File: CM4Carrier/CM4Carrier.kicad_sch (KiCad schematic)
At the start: 0 parts

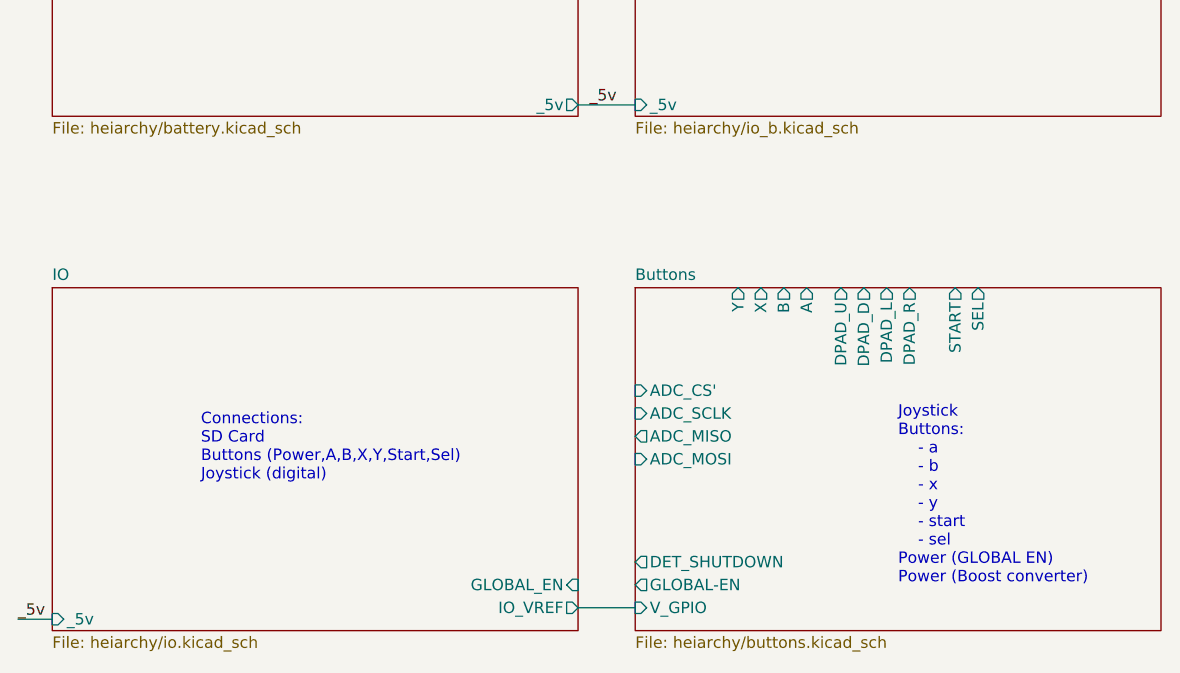
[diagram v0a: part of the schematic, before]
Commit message: footprints  + values
need to do some 3d babeeeeeeeeee
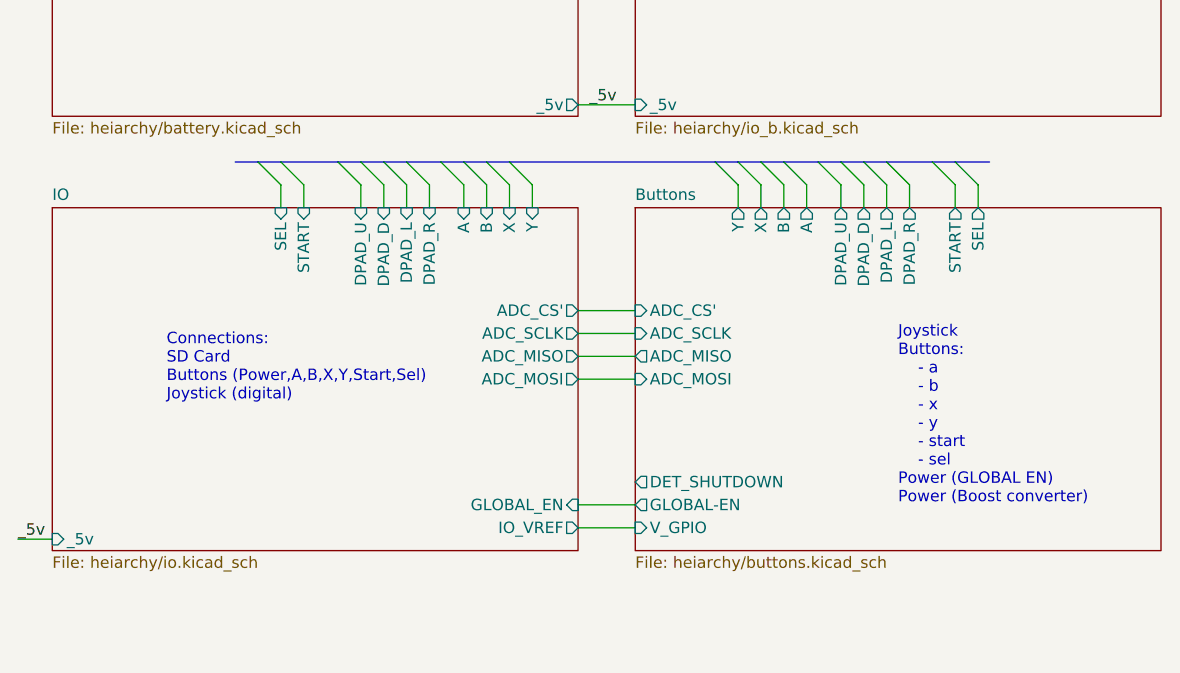
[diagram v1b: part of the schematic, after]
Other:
- sheet IO ports: added A, ADC_CS', ADC_MISO, ADC_MOSI, ADC_SCLK, B, DPAD_D, DPAD_L, DPAD_R, DPAD_U, SEL, START, X, Y; removed none

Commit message: pcb babeee les goooo
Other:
- sheet Battery ports: added ALRT, BATT, FUEL_SCL, FUEL_SDA; removed EN
- sheet Buttons ports: added BATT; removed none
- sheet IO ports: added FUEL_ALRT, FUEL_SCLK, FUEL_SDA; removed none
- sheet IO B ports: added _3.3v; removed none
- title: (none) -> Cm4 battery carrier

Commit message: pcb w proper design
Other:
- note added: "TBF: HEADPHONE JACK / SOUND"
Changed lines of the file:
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@@
     (effects (font (size 1.27 1.27)) (justify left bottom))
+  )
+  (text "TBF: HEADPHONE JACK / SOUND" (at 33.02 39.37 0)
+    (effects (font (size 5.08 5.08)) (justify left bottom))
   )
   (text "Connections:\nSD Card\nButtons (Power,A,B,X,Y,Start,Sel)\nJoystick (digital)\n"

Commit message: LAYOUT DONE!!
:)
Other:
- sheet Battery ports: added BATT_SYSTEM; removed BATT
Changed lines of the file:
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@@
     (stroke (width 0) (type default) (color 0 0 0 0))
   )
-  (wire (pts (xy 152.4 127) (xy 157.48 127))
+  (wire (pts (xy 151.13 127) (xy 157.48 127))
     (stroke (width 0) (type default) (color 0 0 0 0))
   )
@@
     (stroke (width 0) (type default) (color 0 0 0 0))
   )
-  (wire (pts (xy 87.63 49.53) (xy 92.71 49.53))
+  (wire (pts (xy 85.09 49.53) (xy 92.71 49.53))
     (stroke (width 0) (type default) (color 0 0 0 0))
   )
@@
     (effects (font (size 1.27 1.27)) (justify left bottom))
   )
-  (label "BATT" (at 87.63 49.53 0)
+  (label "BATT_S" (at 85.09 49.53 0)
     (effects (font (size 1.27 1.27)) (justify left bottom))
   )
@@
     (effects (font (size 1.27 1.27)) (justify left bottom))
   )
-  (label "BATT" (at 152.4 127 0)
+  (label "BATT_S" (at 151.13 127 0)
     (effects (font (size 1.27 1.27)) (justify left bottom))
   )
@@
       (effects (font (size 1.27 1.27)) (justify left))
     )
-    (pin "BATT" output (at 92.71 49.53 180)
+    (pin "BATT_SYSTEM" output (at 92.71 49.53 180)
       (effects (font (size 1.27 1.27)) (justify left))
     )
@@
       (reference "#PWR042") (unit 1) (value "GND") (footprint "")
     )
+    (path "/1d948cd0-f6e4-4bae-aaaf-c0cfc5cdd7a9/1c3ebfff-ac3c-480a-9097-6cb2c8497089"
+      (reference "#PWR043") (unit 1) (value "GND") (footprint "")
+    )
+    (path "/1d948cd0-f6e4-4bae-aaaf-c0cfc5cdd7a9/39896e95-d5b7-4b2d-91fb-a97d46123782"
+      (reference "#PWR044") (unit 1) (value "GND") (footprint "")
+    )
+    (path "/1d948cd0-f6e4-4bae-aaaf-c0cfc5cdd7a9/731119db-1eb9-4e2e-bea2-451b639aa99a"
+      (reference "#PWR045") (unit 1) (value "GND") (footprint "")
+    )
+    (path "/1d948cd0-f6e4-4bae-aaaf-c0cfc5cdd7a9/1903e911-890a-44bf-8598-6b1ee7a5bdce"
+      (reference "#PWR046") (unit 1) (value "GND") (footprint "")
+    )
+    (path "/1d948cd0-f6e4-4bae-aaaf-c0cfc5cdd7a9/db5d7e63-27d7-4aee-825c-495c36afbd19"
+      (reference "#PWR047") (unit 1) (value "GND") (footprint "")
+    )
+    (path "/1d948cd0-f6e4-4bae-aaaf-c0cfc5cdd7a9/79bcb133-de19-416c-99f3-128fc72d420c"
+      (reference "#PWR048") (unit 1) (value "GND") (footprint "")
+    )
     (path "/a75f8253-7851-4062-bd61-8fb400fa95f7/00a2f2b5-14aa-4afd-bced-d3d12e759a23"
       (reference "BT1") (unit 1) (value "Battery_Cell") (footprint "Connector_JST:JST_XH_S2B-XH-A_1x02_P2.50mm_Horizontal")
@@
       (reference "C26") (unit 1) (value "100n") (footprint "Capacitor_SMD:C_0805_2012Metric_Pad1.18x1.45mm_HandSolder")
     )
+    (path "/1d948cd0-f6e4-4bae-aaaf-c0cfc5cdd7a9/b2cd5d1f-ca21-48bf-babb-dc1a8f95ae47"
+      (reference "C27") (unit 1) (value "C") (footprint "Capacitor_SMD:C_0805_2012Metric_Pad1.18x1.45mm_HandSolder")
+    )
+    (path "/1d948cd0-f6e4-4bae-aaaf-c0cfc5cdd7a9/e6767d3a-d227-419d-91dc-026b3d9dac29"
+      (reference "C28") (unit 1) (value "C") (footprint "Capacitor_SMD:C_0805_2012Metric_Pad1.18x1.45mm_HandSolder")
+    )
+    (path "/1d948cd0-f6e4-4bae-aaaf-c0cfc5cdd7a9/6f6ec9fc-4a4d-464c-abce-93b8e52dde1a"
+      (reference "C29") (unit 1) (value "C") (footprint "Capacitor_SMD:C_0805_2012Metric_Pad1.18x1.45mm_HandSolder")
+    )
+    (path "/1d948cd0-f6e4-4bae-aaaf-c0cfc5cdd7a9/c6deeb5d-77bf-402c-b065-b32a672f9056"
+      (reference "C30") (unit 1) (value "C") (footprint "Capacitor_SMD:C_0805_2012Metric_Pad1.18x1.45mm_HandSolder")
+    )
     (path "/1d948cd0-f6e4-4bae-aaaf-c0cfc5cdd7a9/add2ec1a-64b9-48a2-bba1-4678fd4426b1"
       (reference "D1") (unit 1) (value "LED") (footprint "LED_SMD:LED_0805_2012Metric_Pad1.15x1.40mm_HandSolder")
@@
       (reference "D3") (unit 1) (value "LED") (footprint "LED_SMD:LED_0805_2012Metric_Pad1.15x1.40mm_HandSolder")
     )
+    (path "/1d948cd0-f6e4-4bae-aaaf-c0cfc5cdd7a9/d2d6c656-f950-4157-87a5-63cde50ab906"
+      (reference "D4") (unit 1) (value "BAV99S") (footprint "Package_TO_SOT_SMD:SOT-363_SC-70-6")
+    )
+    (path "/1d948cd0-f6e4-4bae-aaaf-c0cfc5cdd7a9/e87d6291-d889-4bca-99b4-4ea1e6c6bd38"
+      (reference "D4") (unit 2) (value "BAV99S") (footprint "Package_TO_SOT_SMD:SOT-363_SC-70-6")
+    )
     (path "/1d948cd0-f6e4-4bae-aaaf-c0cfc5cdd7a9/6010d012-214c-4430-877c-5992786f91c0"
       (reference "J1") (unit 1) (value "Micro_SD_Card") (footprint "CM4IO:GCT_MEM2067-02-180-00-A_REVB")
@@
       (reference "J5") (unit 1) (value "1-84952-5") (footprint "CM4IO:TE_1-84952-5")
     )
+    (path "/1d948cd0-f6e4-4bae-aaaf-c0cfc5cdd7a9/38ac0130-dea2-4904-9c77-6b6c807f794f"
+      (reference "J6") (unit 1) (value "AudioJack3_Dual_Ground_Switch") (footprint "Connector_Audio:Jack_3.5mm_CUI_SJ-3524-SMT_Horizontal")
+    )
     (path "/a75f8253-7851-4062-bd61-8fb400fa95f7/22500fa5-ec3f-43b8-b073-b8a485720681"
       (reference "L1") (unit 1) (value "0.47u") (footprint "Inductor_SMD:L_1008_2520Metric_Pad1.43x2.20mm_HandSolder")
@@
       (reference "R38") (unit 1) (value "nc") (footprint "Resistor_SMD:R_0805_2012Metric_Pad1.20x1.40mm_HandSolder")
     )
+    (path "/1d948cd0-f6e4-4bae-aaaf-c0cfc5cdd7a9/c4a10c80-a780-41b4-bb7f-cb081f13cb1f"
+      (reference "R39") (unit 1) (value "R") (footprint "Resistor_SMD:R_0805_2012Metric_Pad1.20x1.40mm_HandSolder")
+    )
+    (path "/1d948cd0-f6e4-4bae-aaaf-c0cfc5cdd7a9/55ce97d2-9972-4d19-b3c1-506993631f1d"
+      (reference "R40") (unit 1) (value "R") (footprint "Resistor_SMD:R_0805_2012Metric_Pad1.20x1.40mm_HandSolder")
+    )
+    (path "/1d948cd0-f6e4-4bae-aaaf-c0cfc5cdd7a9/20795852-5961-4a1e-a58a-e018f5fafd6c"
+      (reference "R41") (unit 1) (value "R") (footprint "Resistor_SMD:R_0805_2012Metric_Pad1.20x1.40mm_HandSolder")
+    )
+    (path "/1d948cd0-f6e4-4bae-aaaf-c0cfc5cdd7a9/438822c6-6002-4506-8be6-1c0133b2e53a"
+      (reference "R42") (unit 1) (value "R") (footprint "Resistor_SMD:R_0805_2012Metric_Pad1.20x1.40mm_HandSolder")
+    )
     (path "/fbd4ebba-c181-4efc-9928-2457cd7bdbdb/4bf36d9a-61f9-4997-86b1-0cd76613249d"
       (reference "SW1") (unit 1) (value "SW_Push") (footprint "CM4IO:SW_PTS526_SMG15_SMTR2_LFS")
@@
     )
     (path "/fbd4ebba-c181-4efc-9928-2457cd7bdbdb/fd2605d7-a46a-4354-8d8e-3fff3b7fe671"
-      (reference "U5") (unit 1) (value "74HC00") (footprint "Package_DIP:DIP-14_W7.62mm_Socket_LongPads")
+      (reference "U5") (unit 1) (value "74HC00") (footprint "Package_SO:SOIC-14_3.9x8.7mm_P1.27mm")
     )
     (path "/fbd4ebba-c181-4efc-9928-2457cd7bdbdb/865384e1-8776-433f-8420-1be45ec75c76"
-      (reference "U5") (unit 2) (value "74HC00") (footprint "Package_DIP:DIP-14_W7.62mm_Socket_LongPads")
+      (reference "U5") (unit 2) (value "74HC00") (footprint "Package_SO:SOIC-14_3.9x8.7mm_P1.27mm")
     )
     (path "/fbd4ebba-c181-4efc-9928-2457cd7bdbdb/b2821331-1d98-4eff-88b9-dbc4fa7c7290"
-      (reference "U5") (unit 3) (value "74HC00") (footprint "Package_DIP:DIP-14_W7.62mm_Socket_LongPads")
+      (reference "U5") (unit 3) (value "74HC00") (footprint "Package_SO:SOIC-14_3.9x8.7mm_P1.27mm")
     )
     (path "/fbd4ebba-c181-4efc-9928-2457cd7bdbdb/e71894a1-148d-4541-a93a-51168fe29287"
-      (reference "U5") (unit 4) (value "74HC00") (footprint "Package_DIP:DIP-14_W7.62mm_Socket_LongPads")
+      (reference "U5") (unit 4) (value "74HC00") (footprint "Package_SO:SOIC-14_3.9x8.7mm_P1.27mm")
     )
     (path "/fbd4ebba-c181-4efc-9928-2457cd7bdbdb/50b85a3f-d9fc-47eb-adf8-37c96de60746"
-      (reference "U5") (unit 5) (value "74HC00") (footprint "Package_DIP:DIP-14_W7.62mm_Socket_LongPads")
+      (reference "U5") (unit 5) (value "74HC00") (footprint "Package_SO:SOIC-14_3.9x8.7mm_P1.27mm")
     )
     (path "/fbd4ebba-c181-4efc-9928-2457cd7bdbdb/93ed32cf-1bd7-4696-9a77-613fa11c649c"
-      (reference "U6") (unit 1) (value "MCP3002") (footprint "Package_DIP:DIP-8_W7.62mm_LongPads")
-    )
-  )
+      (reference "U6") (unit 1) (value "MCP3002") (footprint "Package_SO:TSSOP-8_4.4x3mm_P0.65mm")
+    )
+  )
